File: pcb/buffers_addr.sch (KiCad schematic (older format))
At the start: 24 parts, among them U3 74LVCH162245A, U4 74LVCH162245A

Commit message: more footprints assigned, caps added into open collector base circuit
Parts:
- C5, C6: value 0.1uF -> 0.1uF 35V; footprint (none) -> Capacitor_SMD:C_0603_1608Metric_Pad1.05x0.95mm_HandSolder
- C7, C8: value 10uF -> 10uF 35V; footprint (none) -> Capacitor_SMD:C_1210_3225Metric_Pad1.42x2.65mm_HandSolder
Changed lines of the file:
@@
 P 3250 5600
 F 0 "C7" V 3502 5600 50  0000 C CNN
-F 1 "10uF" V 3411 5600 50  0000 C CNN
-F 2 "" H 3288 5450 50  0001 C CNN
+F 1 "10uF 35V" V 3411 5600 50  0000 C CNN
+F 2 "Capacitor_SMD:C_1210_3225Metric_Pad1.42x2.65mm_HandSolder" H 3288 5450 50  0001 C CNN
 F 3 "~" H 3250 5600 50  0001 C CNN
 	1    3250 5600
@@
 P 3250 5200
 F 0 "C5" V 3502 5200 50  0000 C CNN
-F 1 "0.1uF" V 3411 5200 50  0000 C CNN
-F 2 "" H 3288 5050 50  0001 C CNN
+F 1 "0.1uF 35V" V 3411 5200 50  0000 C CNN
+F 2 "Capacitor_SMD:C_0603_1608Metric_Pad1.05x0.95mm_HandSolder" H 3288 5050 50  0001 C CNN
 F 3 "~" H 3250 5200 50  0001 C CNN
 	1    3250 5200
@@
 P 8050 5600
 F 0 "C8" V 8302 5600 50  0000 C CNN
-F 1 "10uF" V 8211 5600 50  0000 C CNN
-F 2 "" H 8088 5450 50  0001 C CNN
+F 1 "10uF 35V" V 8211 5600 50  0000 C CNN
+F 2 "Capacitor_SMD:C_1210_3225Metric_Pad1.42x2.65mm_HandSolder" H 8088 5450 50  0001 C CNN
 F 3 "~" H 8050 5600 50  0001 C CNN
 	1    8050 5600
@@
 P 8050 5200
 F 0 "C6" V 8302 5200 50  0000 C CNN
-F 1 "0.1uF" V 8211 5200 50  0000 C CNN
-F 2 "" H 8088 5050 50  0001 C CNN
+F 1 "0.1uF 35V" V 8211 5200 50  0000 C CNN
+F 2 "Capacitor_SMD:C_0603_1608Metric_Pad1.05x0.95mm_HandSolder" H 8088 5050 50  0001 C CNN
 F 3 "~" H 8050 5200 50  0001 C CNN
 	1    8050 5200

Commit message: working on pcb 2
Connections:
- net labels added: D0, D1, D2, D3, D4, D5, D6, D7, FPGA_D0, FPGA_D1, FPGA_D2, FPGA_D3, FPGA_D4, FPGA_D5, FPGA_D6, FPGA_D7, FPGA_D_BUFF_DIR, _FPGA_D_BUFF_OE
- net labels removed: A0, A1, A2, A3, A4, A5, A6, A7, FPGA_A0, FPGA_A1, FPGA_A2, FPGA_A3, FPGA_A4, FPGA_A5, FPGA_A6, FPGA_A7
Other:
- moved on the sheet: XT10, XT11, XT12, XT13, XT14, XT15, XT16, XT17, XT18, XT19, XT20, XT5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

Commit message: working on pcb
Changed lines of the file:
@@
 	9700 1850 10000 1850
 Wire Wire Line
-	10000 2150 9700 2150
-Wire Wire Line
-	9700 2250 10000 2250
+	10000 2250 9700 2250
+Wire Wire Line
+	9700 2150 10000 2150
 Wire Wire Line
 	10000 1750 9700 1750
@@
 Text GLabel 10000 2050 2    50   BiDi ~ 0
 _FPGA_AS
+Text GLabel 10000 1850 2    50   BiDi ~ 0
+_FPGA_DS
 Text GLabel 10000 1950 2    50   BiDi ~ 0
-_FPGA_DS
-Text GLabel 10000 1850 2    50   BiDi ~ 0
 FPGA_R_W
+Text GLabel 10000 2250 2    50   BiDi ~ 0
+FPGA_SIZE0
 Text GLabel 10000 2150 2    50   BiDi ~ 0
-FPGA_SIZE0
-Text GLabel 10000 2250 2    50   BiDi ~ 0
 FPGA_SIZE1
 Text GLabel 10000 1750 2    50   BiDi ~ 0
@@
 FPGA_FC0
 Wire Wire Line
-	6250 2250 6450 2250
-Wire Wire Line
-	6450 2150 6250 2150
+	6450 2250 6250 2250
 Wire Wire Line
 	6250 1550 6450 1550
@@
 Text GLabel 6250 1750 0    50   BiDi ~ 0
 FC2
-Text GLabel 6250 2250 0    50   BiDi ~ 0
-SIZE1
-Text GLabel 6250 2150 0    50   BiDi ~ 0
-SIZE0
+Text GLabel 6250 1950 0    50   BiDi ~ 0
+R_W
 Text GLabel 6250 1850 0    50   BiDi ~ 0
-R_W
-Text GLabel 6250 1950 0    50   BiDi ~ 0
 _DS
 Text GLabel 6250 2050 0    50   BiDi ~ 0
@@
 Wire Wire Line
 	7400 3900 6650 3900
+Text GLabel 6250 2250 0    50   BiDi ~ 0
+SIZE0
+Text GLabel 6250 2150 0    50   BiDi ~ 0
+SIZE1
+Wire Wire Line
+	6250 2150 6450 2150
 $EndSCHEMATC

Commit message: Board pcb updated
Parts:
- C7, C8: value 10uF 35V -> 1uF 35V; footprint Capacitor_SMD:C_1210_3225Metric_Pad1.42x2.65mm_HandSolder -> Capacitor_SMD:C_0805_2012Metric_Pad1.15x1.40mm_HandSolder
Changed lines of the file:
@@
 	2300 3900 2600 3900
 Wire Wire Line
-	3950 3800 4250 3800
-Wire Wire Line
-	4250 3900 3950 3900
-Wire Wire Line
-	3950 3600 4250 3600
-Wire Wire Line
-	4250 4100 3950 4100
-Wire Wire Line
-	3950 4200 4250 4200
-Wire Wire Line
-	4250 3700 3950 3700
+	3900 3800 4200 3800
+Wire Wire Line
+	4200 3900 3900 3900
+Wire Wire Line
+	3900 3600 4200 3600
+Wire Wire Line
+	4200 4100 3900 4100
+Wire Wire Line
+	3900 4200 4200 4200
+Wire Wire Line
+	4200 3700 3900 3700
 Wire Wire Line
 	3900 1550 4200 1550
@@
 	4200 2650 3900 2650
 Wire Wire Line
-	3950 3200 4250 3200
-Wire Wire Line
-	4250 3300 3950 3300
-Wire Wire Line
-	3950 3400 4250 3400
-Wire Wire Line
-	4250 3500 3950 3500
+	3900 3200 4200 3200
+Wire Wire Line
+	4200 3300 3900 3300
+Wire Wire Line
+	3900 3400 4200 3400
+Wire Wire Line
+	4200 3500 3900 3500
 Wire Wire Line
 	7400 4100 7300 4100
@@
 P 3250 5600
 F 0 "C7" V 3502 5600 50  0000 C CNN
-F 1 "10uF 35V" V 3411 5600 50  0000 C CNN
-F 2 "Capacitor_SMD:C_1210_3225Metric_Pad1.42x2.65mm_HandSolder" H 3288 5450 50  0001 C CNN
+F 1 "1uF 35V" V 3411 5600 50  0000 C CNN
+F 2 "Capacitor_SMD:C_0805_2012Metric_Pad1.15x1.40mm_HandSolder" H 3288 5450 50  0001 C CNN
 F 3 "~" H 3250 5600 50  0001 C CNN
 	1    3250 5600
@@
 P 8050 5600
 F 0 "C8" V 8302 5600 50  0000 C CNN
-F 1 "10uF 35V" V 8211 5600 50  0000 C CNN
-F 2 "Capacitor_SMD:C_1210_3225Metric_Pad1.42x2.65mm_HandSolder" H 8088 5450 50  0001 C CNN
+F 1 "1uF 35V" V 8211 5600 50  0000 C CNN
+F 2 "Capacitor_SMD:C_0805_2012Metric_Pad1.15x1.40mm_HandSolder" H 8088 5450 50  0001 C CNN
 F 3 "~" H 8050 5600 50  0001 C CNN
 	1    8050 5600
@@
 Text GLabel 4200 2550 2    50   BiDi ~ 0
 _FPGA_A_BUFF_OE
-Text GLabel 4250 4100 2    50   BiDi ~ 0
+Text GLabel 4200 4100 2    50   BiDi ~ 0
 _FPGA_A_BUFF_OE
 Text GLabel 9000 4100 2    50   BiDi ~ 0
@@
 Text GLabel 2500 6800 0    50   BiDi ~ 0
 _FPGA_A_BUFF_OE
-Text GLabel 4250 4200 2    50   BiDi ~ 0
+Text GLabel 4200 4200 2    50   BiDi ~ 0
 FPGA_A_BUFF_DIR
 Text GLabel 9000 2650 2    50   BiDi ~ 0
@@
 Text GLabel 4200 2250 2    50   BiDi ~ 0
 FPGA_A16
-Text GLabel 4250 3200 2    50   BiDi ~ 0
+Text GLabel 4200 3200 2    50   BiDi ~ 0
 FPGA_A15
-Text GLabel 4250 3300 2    50   BiDi ~ 0
+Text GLabel 4200 3300 2    50   BiDi ~ 0
 FPGA_A14
-Text GLabel 4250 3400 2    50   BiDi ~ 0
+Text GLabel 4200 3400 2    50   BiDi ~ 0
 FPGA_A13
-Text GLabel 4250 3500 2    50   BiDi ~ 0
+Text GLabel 4200 3500 2    50   BiDi ~ 0
 FPGA_A12
-Text GLabel 4250 3600 2    50   BiDi ~ 0
+Text GLabel 4200 3600 2    50   BiDi ~ 0
 FPGA_A11
-Text GLabel 4250 3700 2    50   BiDi ~ 0
+Text GLabel 4200 3700 2    50   BiDi ~ 0
 FPGA_A10
-Text GLabel 4250 3800 2    50   BiDi ~ 0
+Text GLabel 4200 3800 2    50   BiDi ~ 0
 FPGA_A9
-Text GLabel 4250 3900 2    50   BiDi ~ 0
+Text GLabel 4200 3900 2    50   BiDi ~ 0
 FPGA_A8
 Text GLabel 10000 2050 2    50   BiDi ~ 0

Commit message: some more work done
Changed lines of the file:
@@
 Text GLabel 3950 6800 2    50   BiDi ~ 0
 +3V3_BUFFER
-Text GLabel 4200 1550 2    50   BiDi ~ 0
+Text GLabel 4250 1550 2    50   BiDi ~ 0
 FPGA_A23
-Text GLabel 4200 1650 2    50   BiDi ~ 0
+Text GLabel 4250 1650 2    50   BiDi ~ 0
 FPGA_A22
-Text GLabel 4200 1750 2    50   BiDi ~ 0
+Text GLabel 4250 1750 2    50   BiDi ~ 0
 FPGA_A21
-Text GLabel 4200 1850 2    50   BiDi ~ 0
+Text GLabel 4250 1850 2    50   BiDi ~ 0
 FPGA_A20
-Text GLabel 4200 1950 2    50   BiDi ~ 0
+Text GLabel 4250 1950 2    50   BiDi ~ 0
 FPGA_A19
-Text GLabel 4200 2050 2    50   BiDi ~ 0
+Text GLabel 4250 2050 2    50   BiDi ~ 0
 FPGA_A18
-Text GLabel 4200 2150 2    50   BiDi ~ 0
+Text GLabel 4250 2150 2    50   BiDi ~ 0
 FPGA_A17
-Text GLabel 4200 2250 2    50   BiDi ~ 0
+Text GLabel 4250 2250 2    50   BiDi ~ 0
 FPGA_A16
-Text GLabel 4200 3200 2    50   BiDi ~ 0
+Text GLabel 4250 3200 2    50   BiDi ~ 0
 FPGA_A15
-Text GLabel 4200 3300 2    50   BiDi ~ 0
+Text GLabel 4250 3300 2    50   BiDi ~ 0
 FPGA_A14
-Text GLabel 4200 3400 2    50   BiDi ~ 0
+Text GLabel 4250 3400 2    50   BiDi ~ 0
 FPGA_A13
-Text GLabel 4200 3500 2    50   BiDi ~ 0
+Text GLabel 4250 3500 2    50   BiDi ~ 0
 FPGA_A12
-Text GLabel 4200 3600 2    50   BiDi ~ 0
+Text GLabel 4250 3600 2    50   BiDi ~ 0
 FPGA_A11
-Text GLabel 4200 3700 2    50   BiDi ~ 0
+Text GLabel 4250 3700 2    50   BiDi ~ 0
 FPGA_A10
-Text GLabel 4200 3800 2    50   BiDi ~ 0
+Text GLabel 4250 3800 2    50   BiDi ~ 0
 FPGA_A9
-Text GLabel 4200 3900 2    50   BiDi ~ 0
+Text GLabel 4250 3900 2    50   BiDi ~ 0
 FPGA_A8
-Text GLabel 10000 2050 2    50   BiDi ~ 0
+Text GLabel 10050 2050 2    50   BiDi ~ 0
 _FPGA_AS
-Text GLabel 10000 1850 2    50   BiDi ~ 0
+Text GLabel 10050 1850 2    50   BiDi ~ 0
 _FPGA_DS
-Text GLabel 10000 1950 2    50   BiDi ~ 0
+Text GLabel 10050 1950 2    50   BiDi ~ 0
 FPGA_R_W
-Text GLabel 10000 2250 2    50   BiDi ~ 0
+Text GLabel 10050 2250 2    50   BiDi ~ 0
 FPGA_SIZE0
-Text GLabel 10000 2150 2    50   BiDi ~ 0
+Text GLabel 10050 2150 2    50   BiDi ~ 0
 FPGA_SIZE1
-Text GLabel 10000 1750 2    50   BiDi ~ 0
+Text GLabel 10050 1750 2    50   BiDi ~ 0
 FPGA_FC2
-Text GLabel 10000 1650 2    50   BiDi ~ 0
+Text GLabel 10050 1650 2    50   BiDi ~ 0
 FPGA_FC1
-Text GLabel 10000 1550 2    50   BiDi ~ 0
+Text GLabel 10050 1550 2    50   BiDi ~ 0
 FPGA_FC0
 Wire Wire Line
@@
 Text GLabel 6650 3200 0    50   BiDi ~ 0
 D0
-Text GLabel 8950 3900 2    50   BiDi ~ 0
+Text GLabel 9000 3900 2    50   BiDi ~ 0
 FPGA_D7
-Text GLabel 8950 3800 2    50   BiDi ~ 0
+Text GLabel 9000 3800 2    50   BiDi ~ 0
 FPGA_D6
-Text GLabel 8950 3700 2    50   BiDi ~ 0
+Text GLabel 9000 3700 2    50   BiDi ~ 0
 FPGA_D5
-Text GLabel 8950 3600 2    50   BiDi ~ 0
+Text GLabel 9000 3600 2    50   BiDi ~ 0
 FPGA_D4
-Text GLabel 8950 3500 2    50   BiDi ~ 0
+Text GLabel 9000 3500 2    50   BiDi ~ 0
 FPGA_D3
-Text GLabel 8950 3400 2    50   BiDi ~ 0
+Text GLabel 9000 3400 2    50   BiDi ~ 0
 FPGA_D2
-Text GLabel 8950 3300 2    50   BiDi ~ 0
+Text GLabel 9000 3300 2    50   BiDi ~ 0
 FPGA_D1
-Text GLabel 8950 3200 2    50   BiDi ~ 0
+Text GLabel 9000 3200 2    50   BiDi ~ 0
 FPGA_D0
 Text GLabel 6650 3900 0    50   BiDi ~ 0

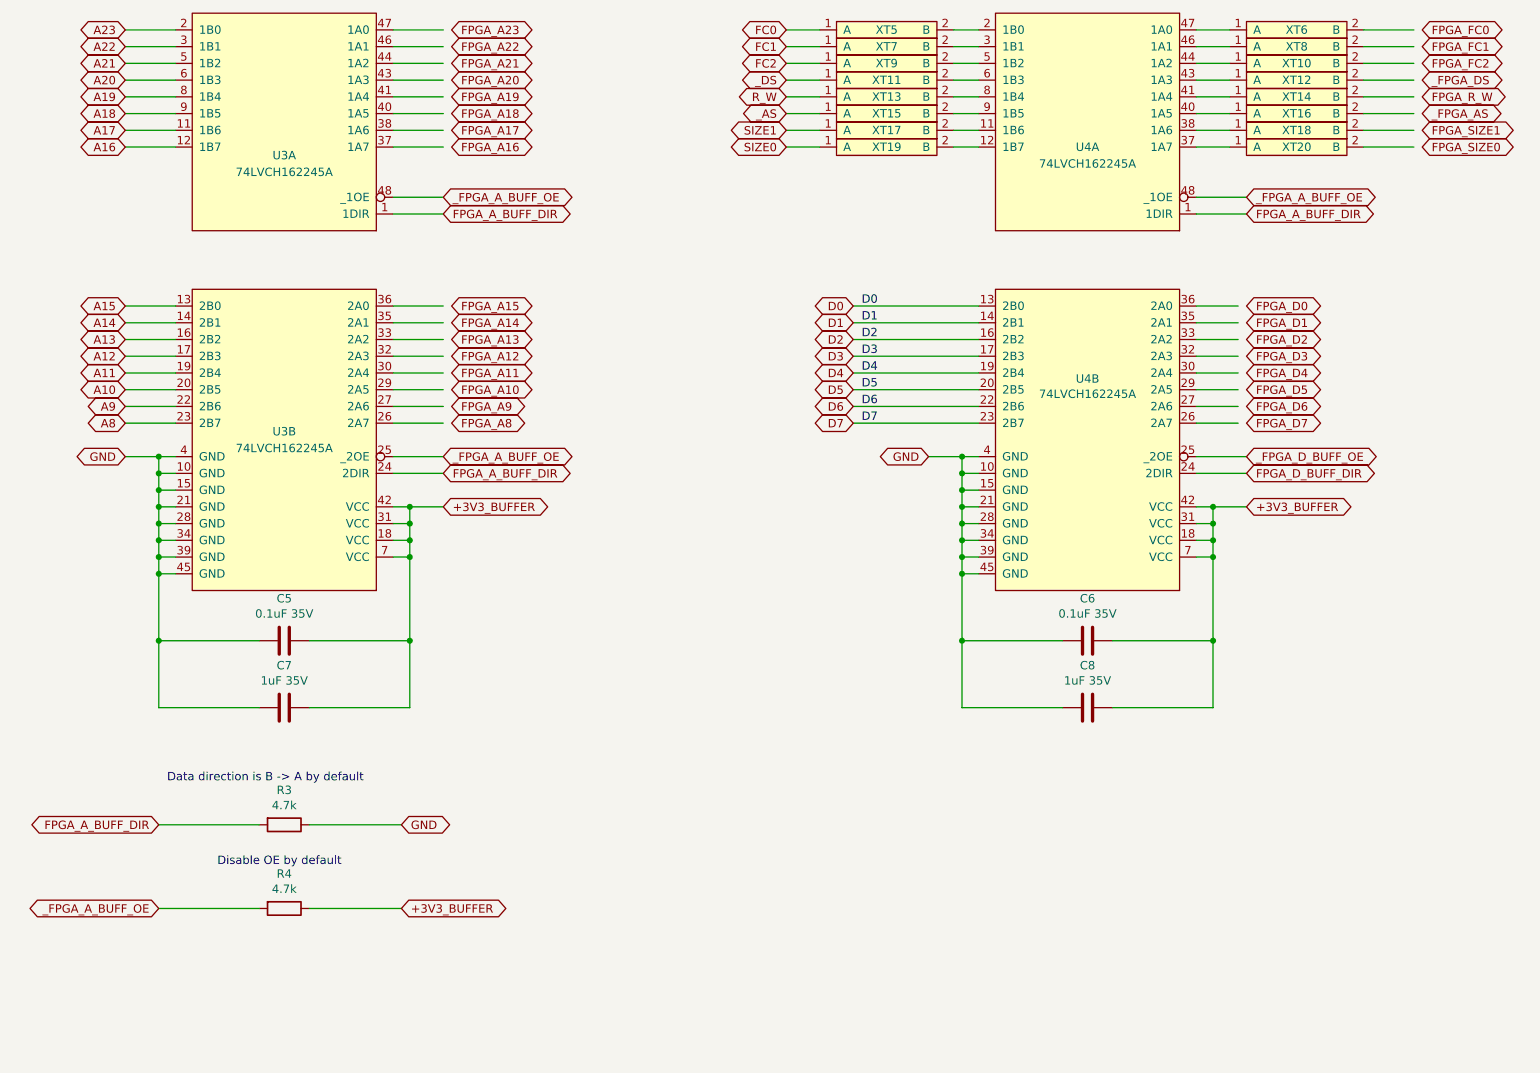
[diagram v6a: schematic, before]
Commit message: Buffers power scheme rework in progress, re-annotate board
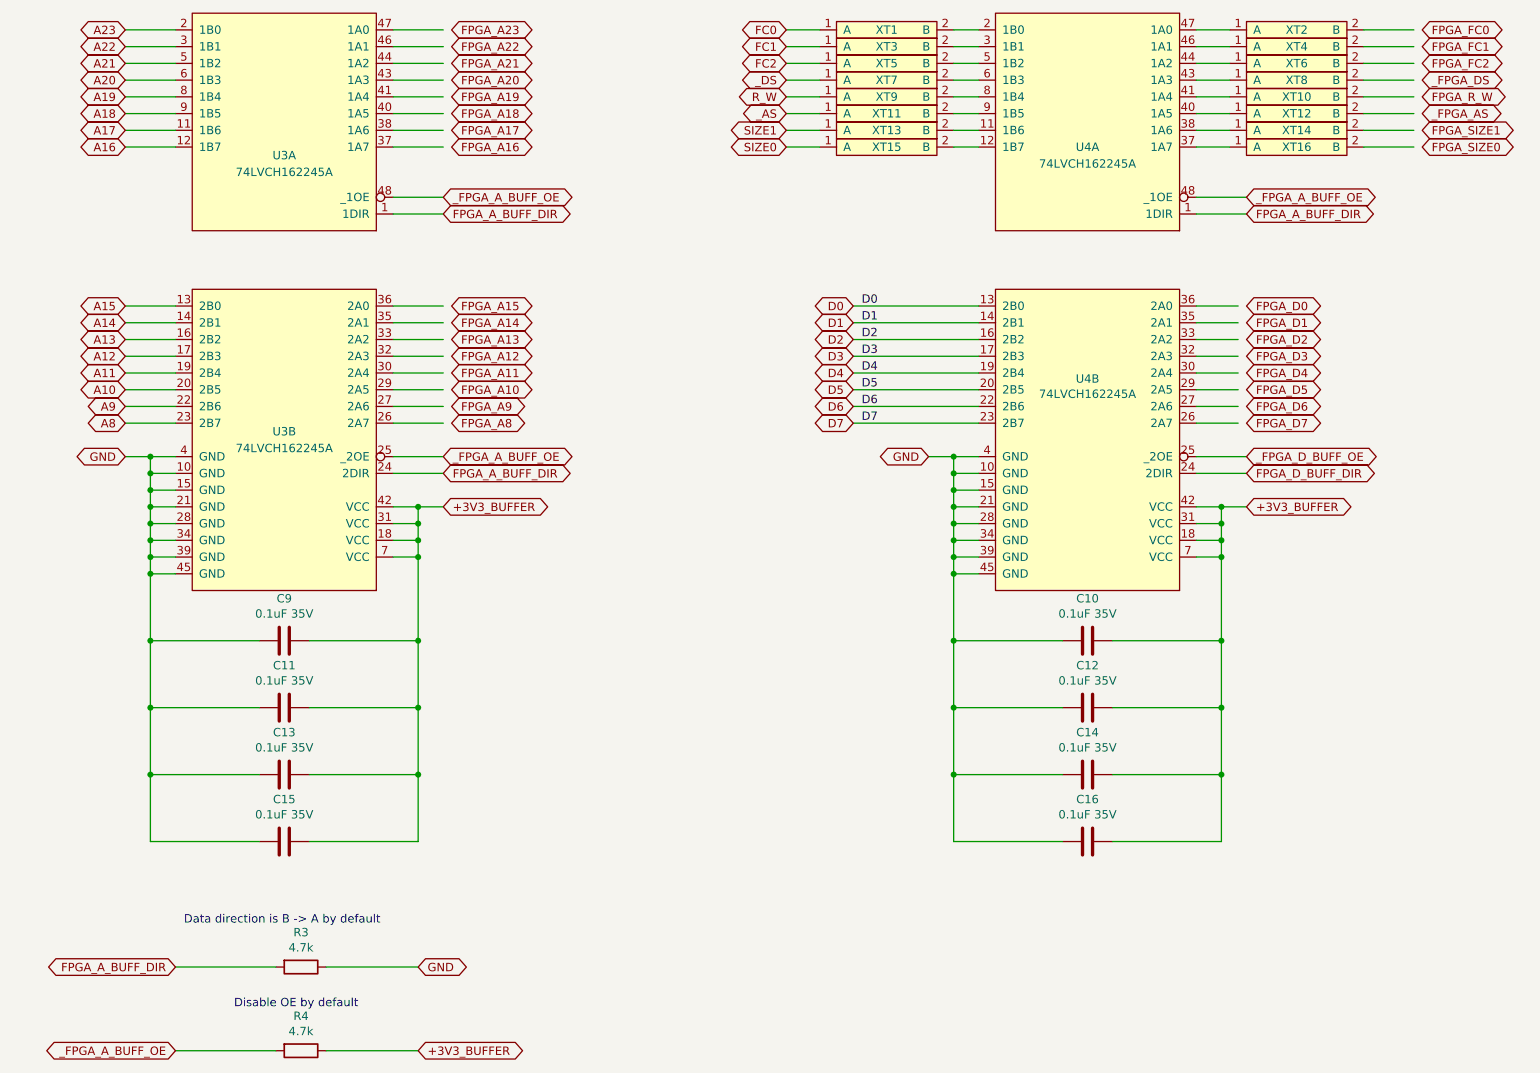
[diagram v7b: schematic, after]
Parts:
- removed C5, C6: 0.1uF 35V, Capacitor_SMD:C_0603_1608Metric_Pad1.05x0.95mm_HandSolder, symbol Device:C
- removed C7, C8: 1uF 35V, Capacitor_SMD:C_0805_2012Metric_Pad1.15x1.40mm_HandSolder, symbol Device:C
- added C10, C11, C12, C13, C14, C15, C16, C9: 0.1uF 35V, Capacitor_SMD:C_0603_1608Metric_Pad1.05x0.95mm_HandSolder, symbol Device:C
- renumbered XT5 to XT1, XT14 to XT10, XT15 to XT11, XT16 to XT12, XT17 to XT13, XT18 to XT14, XT19 to XT15, XT20 to XT16, XT6 to XT2, XT7 to XT3, XT8 to XT4, XT9 to XT5, XT10 to XT6, XT11 to XT7, XT12 to XT8, XT13 to XT9
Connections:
- wire segments 156 -> 172
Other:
- moved on the sheet: R3, R4

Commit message: Some work done, sync
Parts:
- C10, C11, C12, C13, C14, C15, C16, C9: footprint Capacitor_SMD:C_0603_1608Metric_Pad1.05x0.95mm_HandSolder -> Capacitor_SMD:C_0402_1005Metric
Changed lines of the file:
@@
 F 0 "C9" V 3502 5200 50  0000 C CNN
 F 1 "0.1uF 35V" V 3411 5200 50  0000 C CNN
-F 2 "Capacitor_SMD:C_0603_1608Metric_Pad1.05x0.95mm_HandSolder" H 3288 5050 50  0001 C CNN
+F 2 "Capacitor_SMD:C_0402_1005Metric" H 3288 5050 50  0001 C CNN
 F 3 "~" H 3250 5200 50  0001 C CNN
 	1    3250 5200
@@
 F 0 "C11" V 3502 5600 50  0000 C CNN
 F 1 "0.1uF 35V" V 3411 5600 50  0000 C CNN
-F 2 "Capacitor_SMD:C_0603_1608Metric_Pad1.05x0.95mm_HandSolder" H 3288 5450 50  0001 C CNN
+F 2 "Capacitor_SMD:C_0402_1005Metric" H 3288 5450 50  0001 C CNN
 F 3 "~" H 3250 5600 50  0001 C CNN
 	1    3250 5600
@@
 F 0 "C13" V 3502 6000 50  0000 C CNN
 F 1 "0.1uF 35V" V 3411 6000 50  0000 C CNN
-F 2 "Capacitor_SMD:C_0603_1608Metric_Pad1.05x0.95mm_HandSolder" H 3288 5850 50  0001 C CNN
+F 2 "Capacitor_SMD:C_0402_1005Metric" H 3288 5850 50  0001 C CNN
 F 3 "~" H 3250 6000 50  0001 C CNN
 	1    3250 6000
@@
 F 0 "C15" V 3502 6400 50  0000 C CNN
 F 1 "0.1uF 35V" V 3411 6400 50  0000 C CNN
-F 2 "Capacitor_SMD:C_0603_1608Metric_Pad1.05x0.95mm_HandSolder" H 3288 6250 50  0001 C CNN
+F 2 "Capacitor_SMD:C_0402_1005Metric" H 3288 6250 50  0001 C CNN
 F 3 "~" H 3250 6400 50  0001 C CNN
 	1    3250 6400
@@
 F 0 "C10" V 8302 5200 50  0000 C CNN
 F 1 "0.1uF 35V" V 8211 5200 50  0000 C CNN
-F 2 "Capacitor_SMD:C_0603_1608Metric_Pad1.05x0.95mm_HandSolder" H 8088 5050 50  0001 C CNN
+F 2 "Capacitor_SMD:C_0402_1005Metric" H 8088 5050 50  0001 C CNN
 F 3 "~" H 8050 5200 50  0001 C CNN
 	1    8050 5200
@@
 F 0 "C12" V 8302 5600 50  0000 C CNN
 F 1 "0.1uF 35V" V 8211 5600 50  0000 C CNN
-F 2 "Capacitor_SMD:C_0603_1608Metric_Pad1.05x0.95mm_HandSolder" H 8088 5450 50  0001 C CNN
+F 2 "Capacitor_SMD:C_0402_1005Metric" H 8088 5450 50  0001 C CNN
 F 3 "~" H 8050 5600 50  0001 C CNN
 	1    8050 5600
@@
 F 0 "C14" V 8302 6000 50  0000 C CNN
 F 1 "0.1uF 35V" V 8211 6000 50  0000 C CNN
-F 2 "Capacitor_SMD:C_0603_1608Metric_Pad1.05x0.95mm_HandSolder" H 8088 5850 50  0001 C CNN
+F 2 "Capacitor_SMD:C_0402_1005Metric" H 8088 5850 50  0001 C CNN
 F 3 "~" H 8050 6000 50  0001 C CNN
 	1    8050 6000
@@
 F 0 "C16" V 8302 6400 50  0000 C CNN
 F 1 "0.1uF 35V" V 8211 6400 50  0000 C CNN
-F 2 "Capacitor_SMD:C_0603_1608Metric_Pad1.05x0.95mm_HandSolder" H 8088 6250 50  0001 C CNN
+F 2 "Capacitor_SMD:C_0402_1005Metric" H 8088 6250 50  0001 C CNN
 F 3 "~" H 8050 6400 50  0001 C CNN
 	1    8050 6400
